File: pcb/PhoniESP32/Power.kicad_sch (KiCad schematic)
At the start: 30 parts, among them J1 Connector, USB-TYPE-C-16P, J2 Conn_Battery, SW1 SK12D07VG5, U1 TPS631000DRLR, U5 BQ24073RGTR

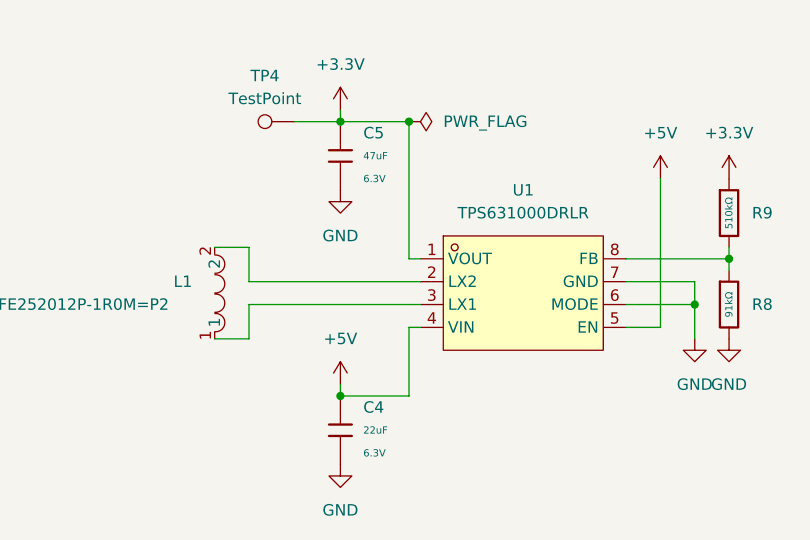
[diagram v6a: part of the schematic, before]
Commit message: chore(pcb): add bigger copper areas for power distribution
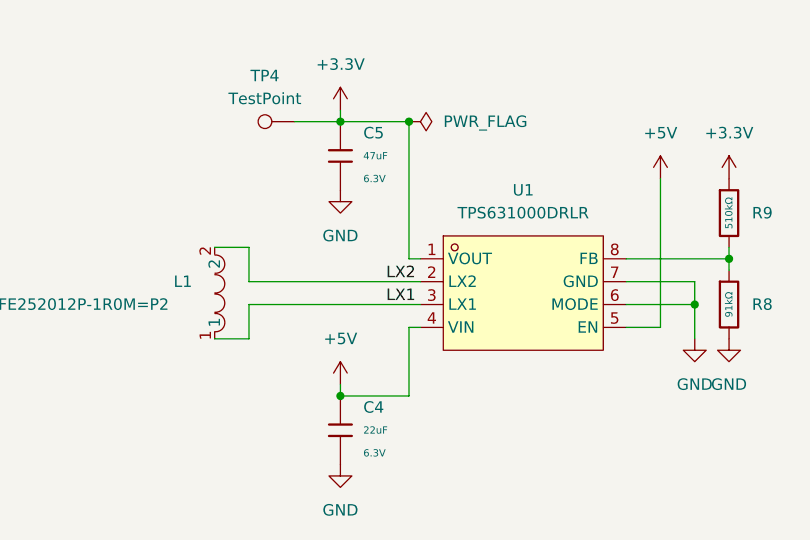
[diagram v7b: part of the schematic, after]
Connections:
- net LX2: now reaches L1.2, U1.2 (LX2)
- net LX1: now reaches L1.1, U1.3 (LX1)
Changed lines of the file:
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@@
+		)
+	)
+	(label "LX2"
+		(at 57.15 146.05 0)
+		(effects
+			(font
+				(size 1.27 1.27)
+			)
+			(justify left bottom)
+		)
+	)
+	(label "LX1"
+		(at 57.15 148.59 0)
+		(effects
+			(font
+				(size 1.27 1.27)
+			)
+			(justify left bottom)
 		)
 	)
